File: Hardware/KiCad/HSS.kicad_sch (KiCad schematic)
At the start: 16 parts, among them U2 TPS27SA08-Q1

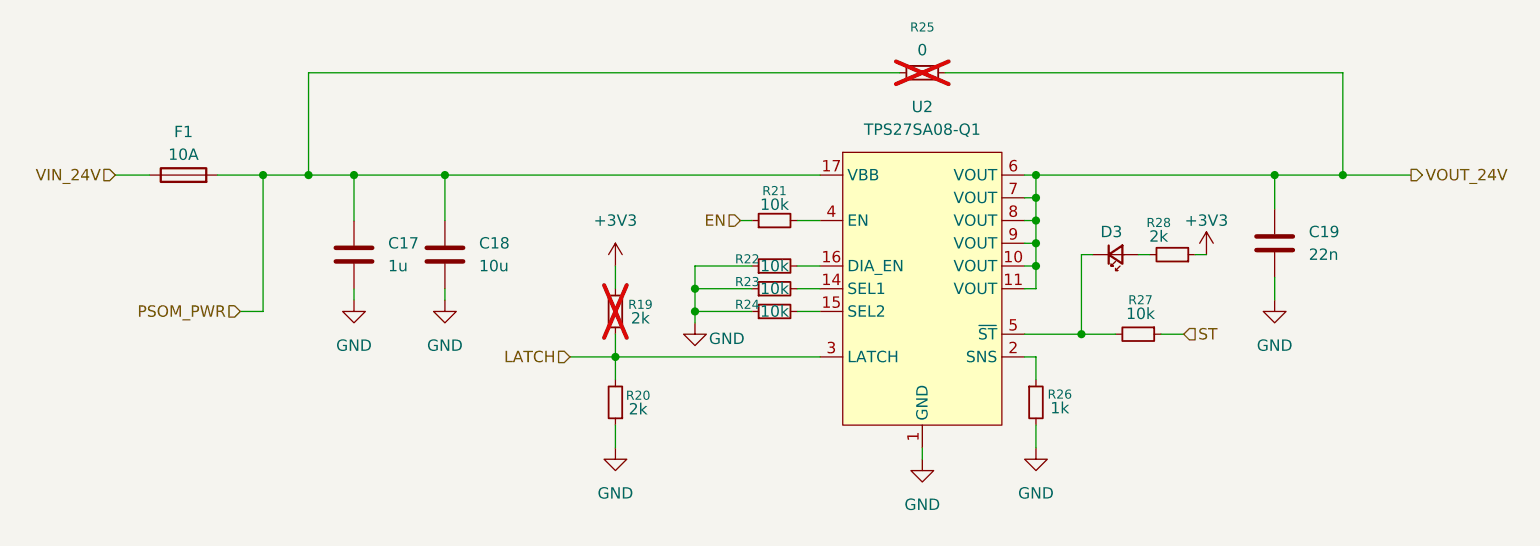
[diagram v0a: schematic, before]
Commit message: layout ready for review
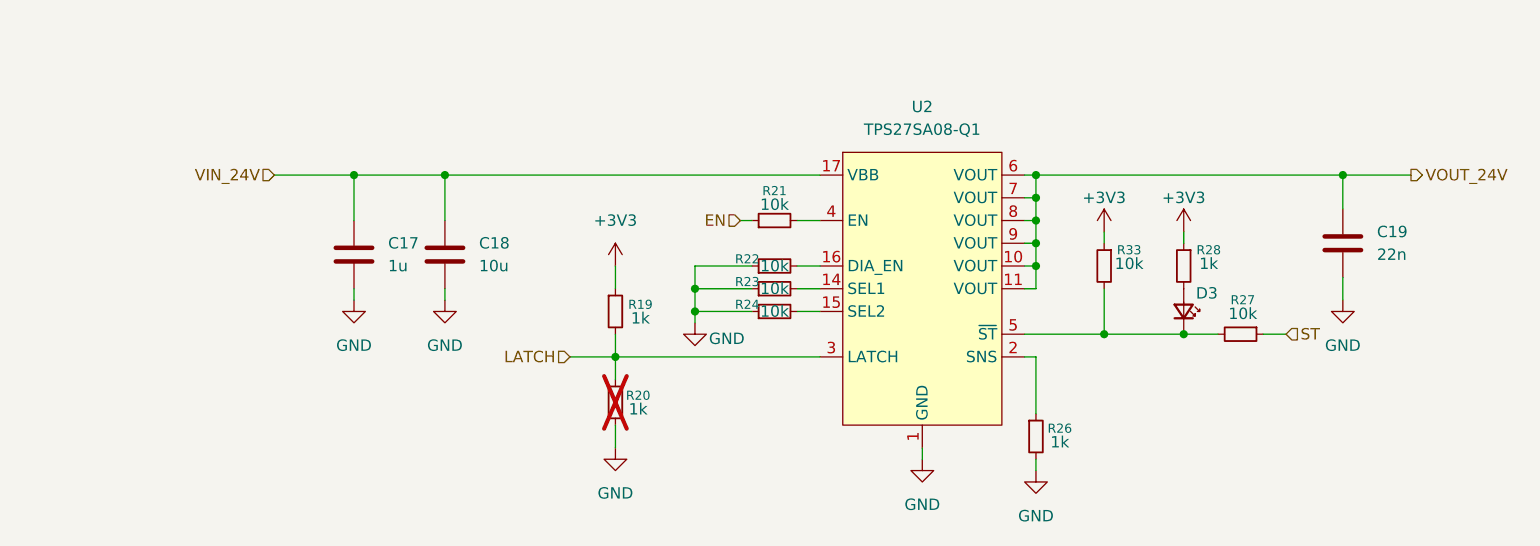
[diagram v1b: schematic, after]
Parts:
- removed F1: 10A, Moco:FUSE_3568, symbol Device:Fuse
- removed R25: 0, Resistor_SMD:R_0603_1608Metric_Pad0.98x0.95mm_HandSolder, symbol Device:R_Small
- added R33: 10k, Resistor_SMD:R_0603_1608Metric_Pad0.98x0.95mm_HandSolder, symbol Device:R_Small
- C17, C18, C19: footprint Capacitor_SMD:C_0805_2012Metric -> Capacitor_SMD:C_0603_1608Metric_Pad1.08x0.95mm_HandSolder
- R19: value 2k -> 1k; now fitted
- R20: value 2k -> 1k; now not fitted
- R28: value 2k -> 1k
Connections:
- net PSOM_PWR is gone; now on net VIN_24V: C17.1, C18.1, U2.17 (VBB)
- net +3V3: now also R33.1
- net at D3.1 (K), R27.2, U2.5 (~{ST}): now also R33.2
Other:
- moved on the sheet: C19, D3, R26, R27, R28

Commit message: layout done
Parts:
- added TP3: TP_ST, TestPoint:TestPoint_Pin_1.0x1.0mm, symbol Connector:TestPoint
- C18: footprint Capacitor_SMD:C_0603_1608Metric_Pad1.08x0.95mm_HandSolder -> Capacitor_SMD:C_0805_2012Metric_Pad1.18x1.45mm_HandSolder
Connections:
- net at D3.1 (K), R27.2, R33.2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: now also TP3.1
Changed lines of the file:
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@@
+	)
+	(junction
+		(at 194.31 105.41)
+		(diameter 0)
+		(color 0 0 0 0)
 	)
 	(junction
@@
 	(wire
 		(pts
-			(xy 189.23 105.41) (xy 198.12 105.41)
+			(xy 189.23 105.41) (xy 194.31 105.41)
 		)
 		(stroke
@@
 		(pts
 			(xy 181.61 95.25) (xy 180.34 95.25)
+		)
+		(stroke
+			(width 0)
+			(type default)
+		)
+	)
+	(wire
+		(pts
+			(xy 194.31 105.41) (xy 198.12 105.41)
 		)
 		(stroke
@@
 	)
 	(symbol
+		(lib_id "Connector:TestPoint")
+		(at 194.31 105.41 0)
+		(unit 1)
+		(exclude_from_sim no)
+		(in_bom no)
+		(on_board yes)
+		(dnp no)
+		(property "Reference" "TP3"
+			(at 193.294 101.092 0)
+			(effects
+				(font
+					(size 1.27 1.27)
+				)
+				(justify right)
+			)
+		)
+		(property "Value" "TP_ST"
+			(at 193.294 103.632 0)
+			(effects
+				(font
+					(size 1.27 1.27)
+				)
+				(justify right)
+			)
+		)
+		(property "Footprint" "TestPoint:TestPoint_Pin_1.0x1.0mm"
+			(at 199.39 105.41 0)
+			(effects
+				(font
+					(size 1.27 1.27)
+				)
+				(hide yes)
+			)
+		)
+		(property "Datasheet" "~"
+			(at 199.39 105.41 0)
+			(effects
+				(font
+					(size 1.27 1.27)
+				)
+				(hide yes)
+			)
+		)
+		(property "Description" "test point"
+			(at 194.31 105.41 0)
+			(effects
+				(font
+					(size 1.27 1.27)
+				)
+				(hide yes)
+			)
+		)
+		(property "Manufacturer" ""
+			(at 194.31 105.41 0)
+			(effects
+				(font
+					(size 1.27 1.27)
+				)
+				(hide yes)
+			)
+		)
+		(property "Mouser Link" ""
+			(at 194.31 105.41 0)
+			(effects
+				(font
+					(size 1.27 1.27)
+				)
+				(hide yes)
+			)
+		)
+		(property "Sim.Type" ""
+			(at 194.31 105.41 0)
+			(effects
+				(font
+					(size 1.27 1.27)
+				)
+				(hide yes)
+			)
+		)
+		(property "Description (Customer #)" ""
+			(at 194.31 105.41 0)
+			(effects
+				(font
+					(size 1.27 1.27)
+				)
+				(hide yes)
+			)
+		)
+		(property "LCSC" ""
+			(at 194.31 105.41 0)
+			(effects
+				(font
+					(size 1.27 1.27)
+				)
+				(hide yes)
+			)
+		)
+		(pin "1"
+		)
+		(instances
+			(project "PS-MotorControllerInterfacePCB"
+				(path "/a2e13c19-ff3a-4e43-a7f5-200fd5b2b978/457b93bf-62f4-46aa-a712-fe00e2990c62"
+					(reference "TP3")
+					(unit 1)
+				)
+			)
+		)
+	)
+	(symbol
 		(lib_id "Device:R_Small")
 		(at 134.62 102.87 0)
@@
 			)
 		)
-		(property "Footprint" "Capacitor_SMD:C_0603_1608Metric_Pad1.08x0.95mm_HandSolder"
+		(property "Footprint" "Capacitor_SMD:C_0805_2012Metric_Pad1.18x1.45mm_HandSolder"
 			(at 116.5352 100.33 0)
 			(effects

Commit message: done with changes
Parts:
- HSS_FAULT1: renamed from TP3; footprint TestPoint:TestPoint_Pin_1.0x1.0mm -> TestPoint:TestPoint_Keystone_5000-5004_Miniature; now in the parts list
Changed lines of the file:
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@@
 	)
 	(hierarchical_label "ST"
-		(shape input)
+		(shape output)
 		(at 209.55 105.41 0)
 		(effects
@@
 		(unit 1)
 		(exclude_from_sim no)
-		(in_bom no)
-		(on_board yes)
-		(dnp no)
-		(property "Reference" "TP3"
+		(in_bom yes)
+		(on_board yes)
+		(dnp no)
+		(property "Reference" "HSS_FAULT1"
 			(at 193.294 101.092 0)
 			(effects
@@
 			)
 		)
-		(property "Footprint" "TestPoint:TestPoint_Pin_1.0x1.0mm"
+		(property "Footprint" "TestPoint:TestPoint_Keystone_5000-5004_Miniature"
 			(at 199.39 105.41 0)
 			(effects
@@
 			(project "PS-MotorControllerInterfacePCB"
 				(path "/a2e13c19-ff3a-4e43-a7f5-200fd5b2b978/457b93bf-62f4-46aa-a712-fe00e2990c62"
-					(reference "TP3")
-					(unit 1)
-				)
+					(reference "HSS_FAULT1")
+					(unit 1)
+				)

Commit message: finished LCSC
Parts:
- C17: LCSC (none) -> C15849
- C18: LCSC (none) -> C440198
- C19: LCSC (none) -> C21122
- D3: LCSC (none) -> C7371904
- HSS_FAULT1: now left out of the parts list
- R19, R20, R26, R28: LCSC (none) -> C21190
- R21, R22, R23, R24, R27, R33: LCSC (none) -> C25804
- U2: LCSC (none) -> C2870129
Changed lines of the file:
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@@
+			)
+		)
+		(property "LCSC" "C25804"
+			(at 152.4 97.79 90)
+			(effects
+				(font
+					(size 1.27 1.27)
+				)
+				(hide yes)
 			)
 		)
@@
 			)
 		)
+		(property "LCSC" "C25804"
+			(at 152.4 92.71 90)
+			(effects
+				(font
+					(size 1.27 1.27)
+				)
+				(hide yes)
+			)
+		)
 		(pin "1"
 		)
@@
 		(property "Description" "Resistor, small symbol"
 			(at 204.47 105.41 0)
+			(effects
+				(font
+					(size 1.27 1.27)
+				)
+				(hide yes)
+			)
+		)
+		(property "LCSC" "C25804"
+			(at 204.47 105.41 90)
 			(effects
 				(font
@@
 			)
 		)
+		(property "LCSC" "C21122"
+			(at 215.9 95.25 0)
+			(effects
+				(font
+					(size 1.27 1.27)
+				)
+				(hide yes)
+			)
+		)
 		(pin "2"
 		)
@@
 			)
 		)
+		(property "LCSC" "C2870129"
+			(at 168.91 100.33 0)
+			(effects
+				(font
+					(size 1.27 1.27)
+				)
+				(hide yes)
+			)
+		)
 		(pin "15"
 		)
@@
 			)
 		)
+		(property "LCSC" "C21190"
+			(at 181.61 116.84 0)
+			(effects
+				(font
+					(size 1.27 1.27)
+				)
+				(hide yes)
+			)
+		)
 		(pin "1"
 		)
@@
 			)
 		)
+		(property "LCSC" "C21190"
+			(at 134.62 113.03 0)
+			(effects
+				(font
+					(size 1.27 1.27)
+				)
+				(hide yes)
+			)
+		)
 		(pin "1"
 		)
@@
 		(unit 1)
 		(exclude_from_sim no)
-		(in_bom yes)
+		(in_bom no)
 		(on_board yes)
 		(dnp no)
@@
 		)
 		(property "Description" "Resistor, small symbol"
+			(at 134.62 102.87 0)
+			(effects
+				(font
+					(size 1.27 1.27)
+				)
+				(hide yes)
+			)
+		)
+		(property "LCSC" "C21190"
 			(at 134.62 102.87 0)
 			(effects
@@
 			)
 		)
+		(property "LCSC" "C25804"
+			(at 189.23 97.79 0)
+			(effects
+				(font
+					(size 1.27 1.27)
+				)
+				(hide yes)
+			)
+		)
 		(pin "1"
 		)
@@
 			)
 		)
+		(property "LCSC" "C440198"
+			(at 115.57 96.52 0)
+			(effects
+				(font
+					(size 1.27 1.27)
+				)
+				(hide yes)
+			)
+		)
 		(pin "2"
 		)
@@
 			)
 		)
+		(property "LCSC" "C21190"
+			(at 198.12 97.79 0)
+			(effects
+				(font
+					(size 1.27 1.27)
+				)
+				(hide yes)
+			)
+		)
 		(pin "1"
 		)
@@
 			)
 		)
+		(property "LCSC" "C15849"
+			(at 105.41 96.52 0)
+			(effects
+				(font
+					(size 1.27 1.27)
+				)
+				(hide yes)
+			)
+		)
 		(pin "2"
 		)
@@
 		(property "Description" "Resistor, small symbol"
 			(at 152.4 102.87 0)
+			(effects
+				(font
+					(size 1.27 1.27)
+				)
+				(hide yes)
+			)
+		)
+		(property "LCSC" "C25804"
+			(at 152.4 102.87 90)
 			(effects
 				(font
@@
 			)
 		)
+		(property "LCSC" "C7371904"
+			(at 198.12 102.87 90)
+			(effects
+				(font
+					(size 1.27 1.27)
+				)
+				(hide yes)
+			)
+		)
 		(pin "1"
 		)
@@
 			(effects
 				(font
+					(size 1.27 1.27)
+				)
+				(hide yes)
+			)
+		)
+		(property "LCSC" "C25804"
+			(at 152.4 100.33 90)
+			(effects
+				(font

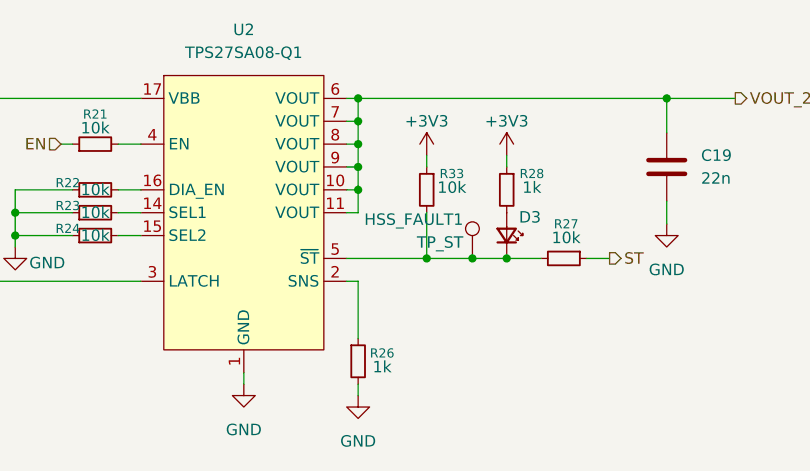
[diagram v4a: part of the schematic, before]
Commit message: fixed references and changed the labels
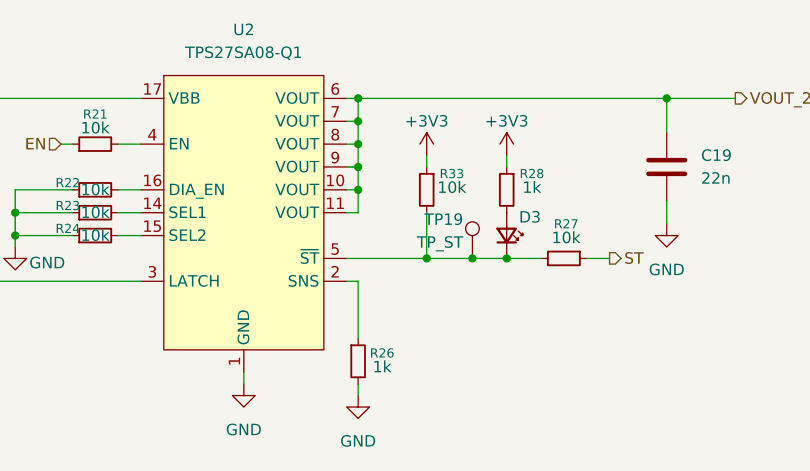
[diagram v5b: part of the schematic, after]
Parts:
- renumbered HSS_FAULT1 to TP19
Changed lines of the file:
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@@
 		(on_board yes)
 		(dnp no)
-		(property "Reference" "HSS_FAULT1"
+		(property "Reference" "TP19"
 			(at 193.294 101.092 0)
 			(effects
@@
 			(project "PS-MotorControllerInterfacePCB"
 				(path "/a2e13c19-ff3a-4e43-a7f5-200fd5b2b978/457b93bf-62f4-46aa-a712-fe00e2990c62"
-					(reference "HSS_FAULT1")
+					(reference "TP19")
 					(unit 1)
 				)

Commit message: standardized some lcsc
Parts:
- D3: LCSC C7371904 -> C84263
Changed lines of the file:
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@@
 			)
 		)
-		(property "LCSC" "C7371904"
+		(property "LCSC" "C84263"
 			(at 198.12 102.87 90)
 			(effects
